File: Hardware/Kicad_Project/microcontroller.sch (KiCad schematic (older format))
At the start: 52 parts

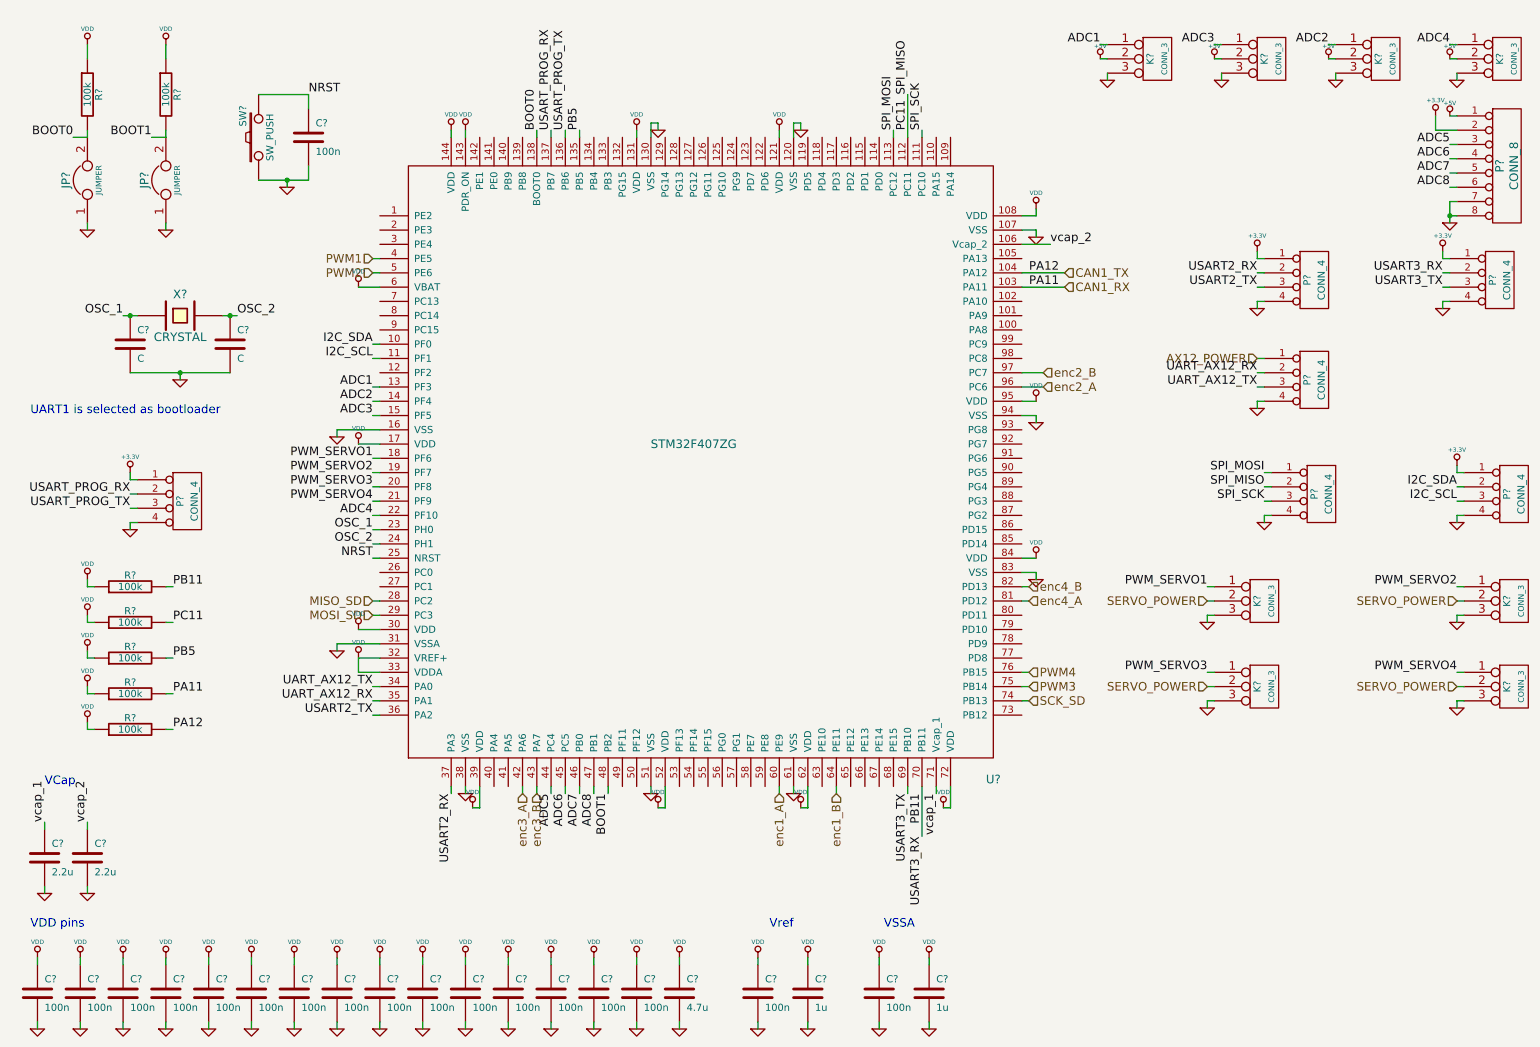
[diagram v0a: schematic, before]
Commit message: [HARDWARE] Add DAC interface
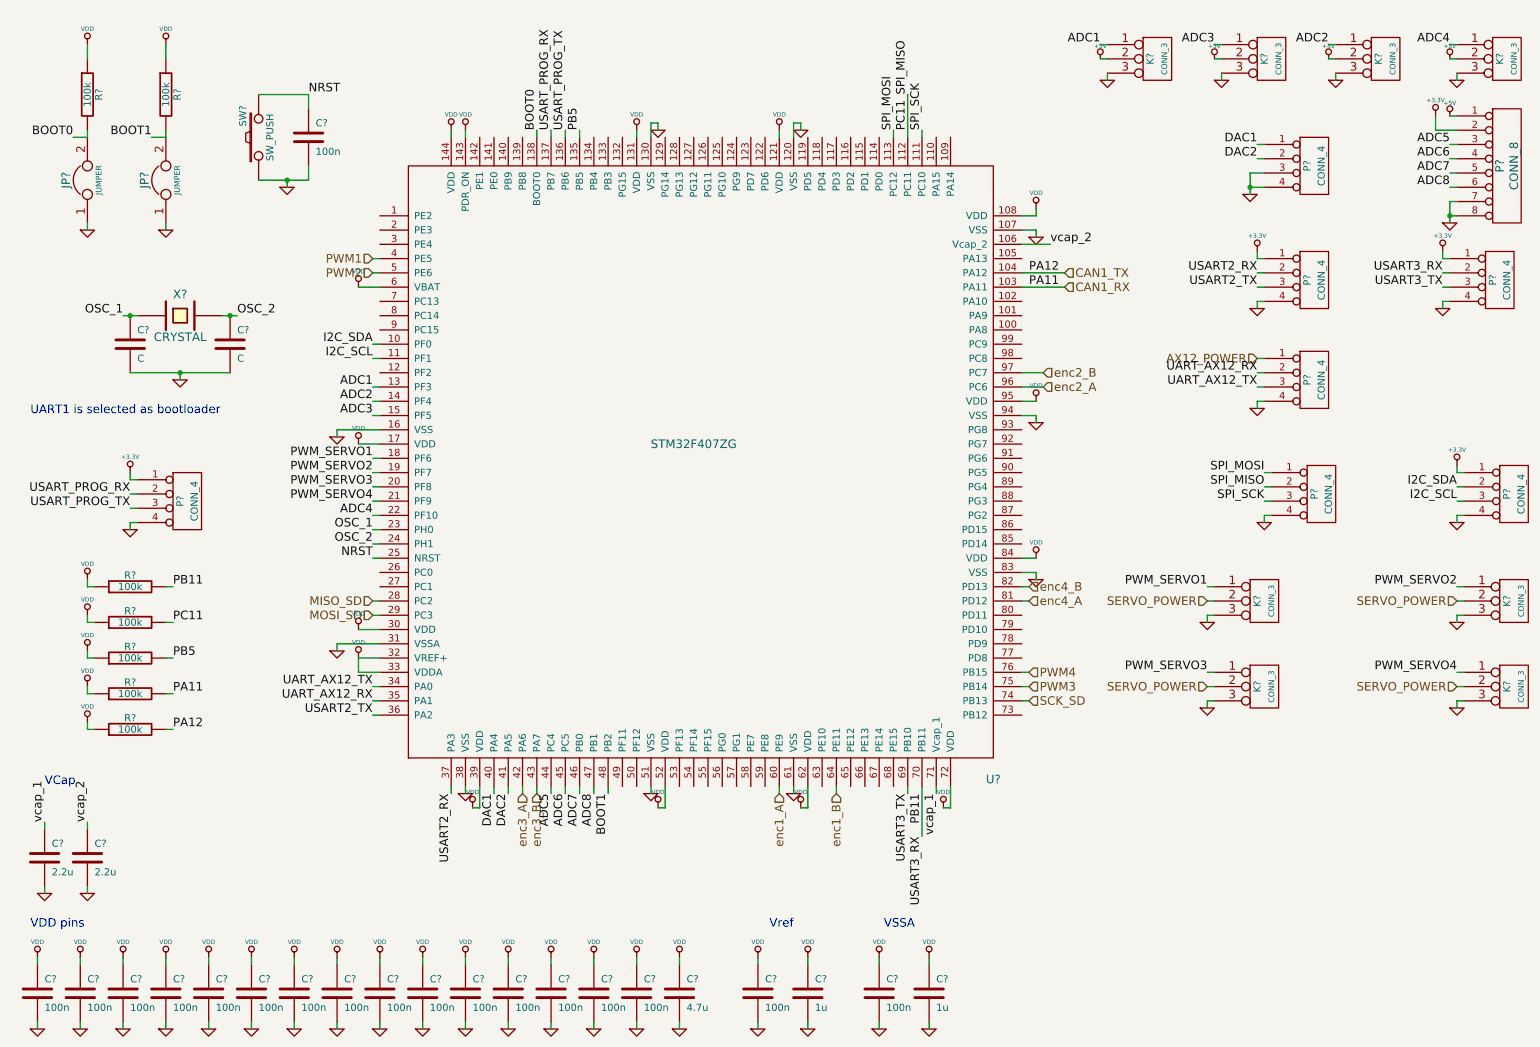
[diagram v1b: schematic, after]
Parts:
- added P?: CONN_4, symbol CONN_4
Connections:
- net GND: now also P?.3 (P3), P?.4 (P4)
- net DAC1: now reaches U?.40 (PA4)
- net DAC1: now also P?.1 (P1)
- net DAC2: now reaches U?.41 (PA5)
- net DAC2: now also P?.2 (P2)
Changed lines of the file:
@@
-EESchema Schematic File Version 2  date mar. 08 oct. 2013 19:30:07 CEST
+EESchema Schematic File Version 2  date mar. 08 oct. 2013 19:33:19 CEST
 LIBS:power
 LIBS:device
@@
 Comment4 ""
 $EndDescr
+Wire Wire Line
+	9150 1500 9200 1500
+Connection ~ 9100 1800
+Wire Wire Line
+	9100 1800 9200 1800
+Wire Wire Line
+	3900 6050 3900 6000
 Connection ~ 10500 2000
 Wire Wire Line
@@
 Wire Wire Line
 	10500 1900 10550 1900
+Wire Wire Line
+	3800 6050 3800 6000
+Wire Wire Line
+	9100 1850 9100 1700
+Wire Wire Line
+	9100 1700 9200 1700
+Wire Wire Line
+	9150 1600 9200 1600
 $Comp
 L GND #PWR?
+U 1 1 525441BE
+P 9100 1850
+F 0 "#PWR?" H 9100 1850 30  0001 C CNN
+F 1 "GND" H 9100 1780 30  0001 C CNN
+	1    9100 1850
+	1    0    0    -1
+$EndComp
+Text Label 9150 1600 2    60   ~ 0
+DAC2
+Text Label 9150 1500 2    60   ~ 0
+DAC1
+$Comp
+L CONN_4 P?
+U 1 1 525441AE
+P 9550 1650
+F 0 "P?" V 9500 1650 50  0000 C CNN
+F 1 "CONN_4" V 9600 1650 50  0000 C CNN
+	1    9550 1650
+	1    0    0    -1
+$EndComp
+Text Label 3900 6050 3    60   ~ 0
+DAC2
+Text Label 3800 6050 3    60   ~ 0
+DAC1
+$Comp
+L GND #PWR?

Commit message: [HARDWARE] Add motor control signals around STM32
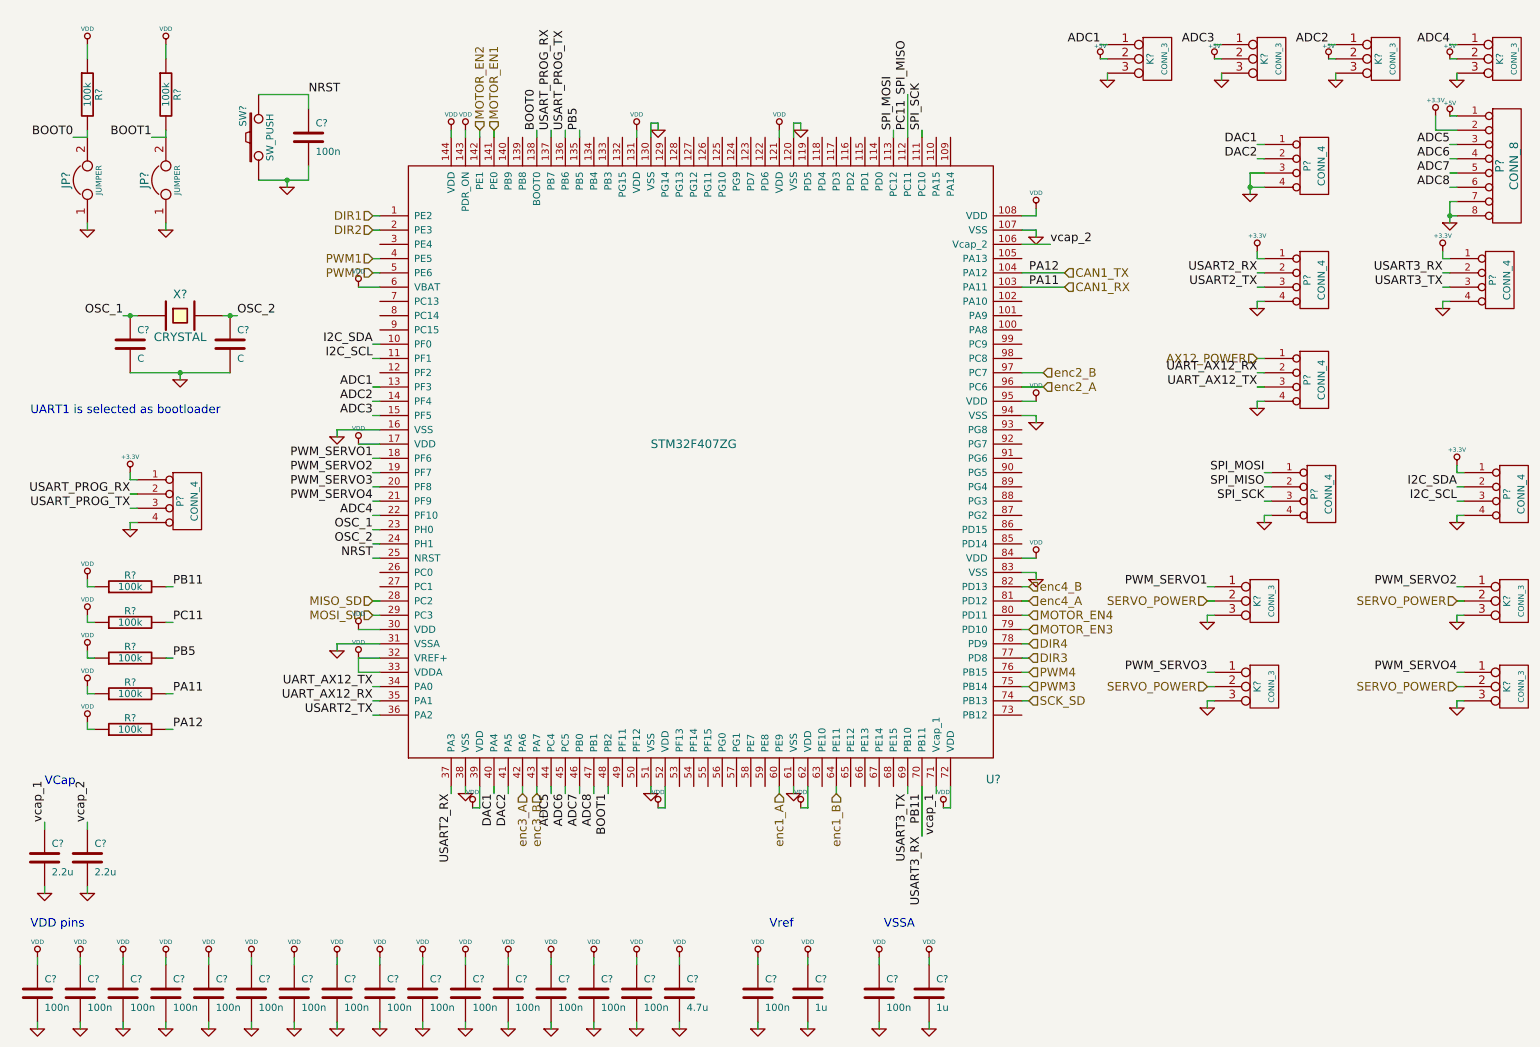
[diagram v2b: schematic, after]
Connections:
- net DIR1: now reaches U?.1 (PE2)
- net MOTOR_EN1: now reaches U?.141 (PE0)
- net MOTOR_EN2: now reaches U?.142 (PE1)
- net DIR2: now reaches U?.2 (PE3)
- net DIR3: now reaches U?.77 (PD8)
- net DIR4: now reaches U?.78 (PD9)
- net MOTOR_EN3: now reaches U?.79 (PD10)
- net MOTOR_EN4: now reaches U?.80 (PD11)
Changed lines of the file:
@@
-EESchema Schematic File Version 2  date mar. 08 oct. 2013 19:33:19 CEST
+EESchema Schematic File Version 2  date mar. 08 oct. 2013 19:41:25 CEST
 LIBS:power
 LIBS:device
@@
 $Descr A4 11700 8267
 encoding utf-8
-Sheet 5 5
+Sheet 2 5
 Title ""
 Date "8 oct 2013"
@@
 $EndDescr
 Wire Wire Line
+	7500 5100 7550 5100
+Wire Wire Line
+	7500 4900 7550 4900
+Wire Wire Line
+	3700 1400 3700 1450
+Wire Wire Line
+	2950 2100 3000 2100
+Wire Wire Line
 	9150 1500 9200 1500
 Connection ~ 9100 1800
@@
 Wire Wire Line
 	9150 1600 9200 1600
+Wire Wire Line
+	3000 2000 2950 2000
+Wire Wire Line
+	3800 1400 3800 1450
+Wire Wire Line
+	7550 4800 7500 4800
+Wire Wire Line
+	7550 5000 7500 5000
+Text HLabel 7550 4800 2    60   Input ~ 0
+MOTOR_EN4
+Text HLabel 7550 4900 2    60   Input ~ 0
+MOTOR_EN3
+Text HLabel 7550 5000 2    60   Input ~ 0
+DIR4
+Text HLabel 7550 5100 2    60   Input ~ 0
+DIR3
+Text HLabel 3700 1400 1    60   Input ~ 0
+MOTOR_EN2
+Text HLabel 3800 1400 1    60   Input ~ 0
+MOTOR_EN1
+Text HLabel 2950 2100 0    60   Input ~ 0
+DIR2
+Text HLabel 2950 2000 0    60   Input ~ 0
+DIR1
 $Comp
 L GND #PWR?

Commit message: [HARDWARE] Finalize SD interface
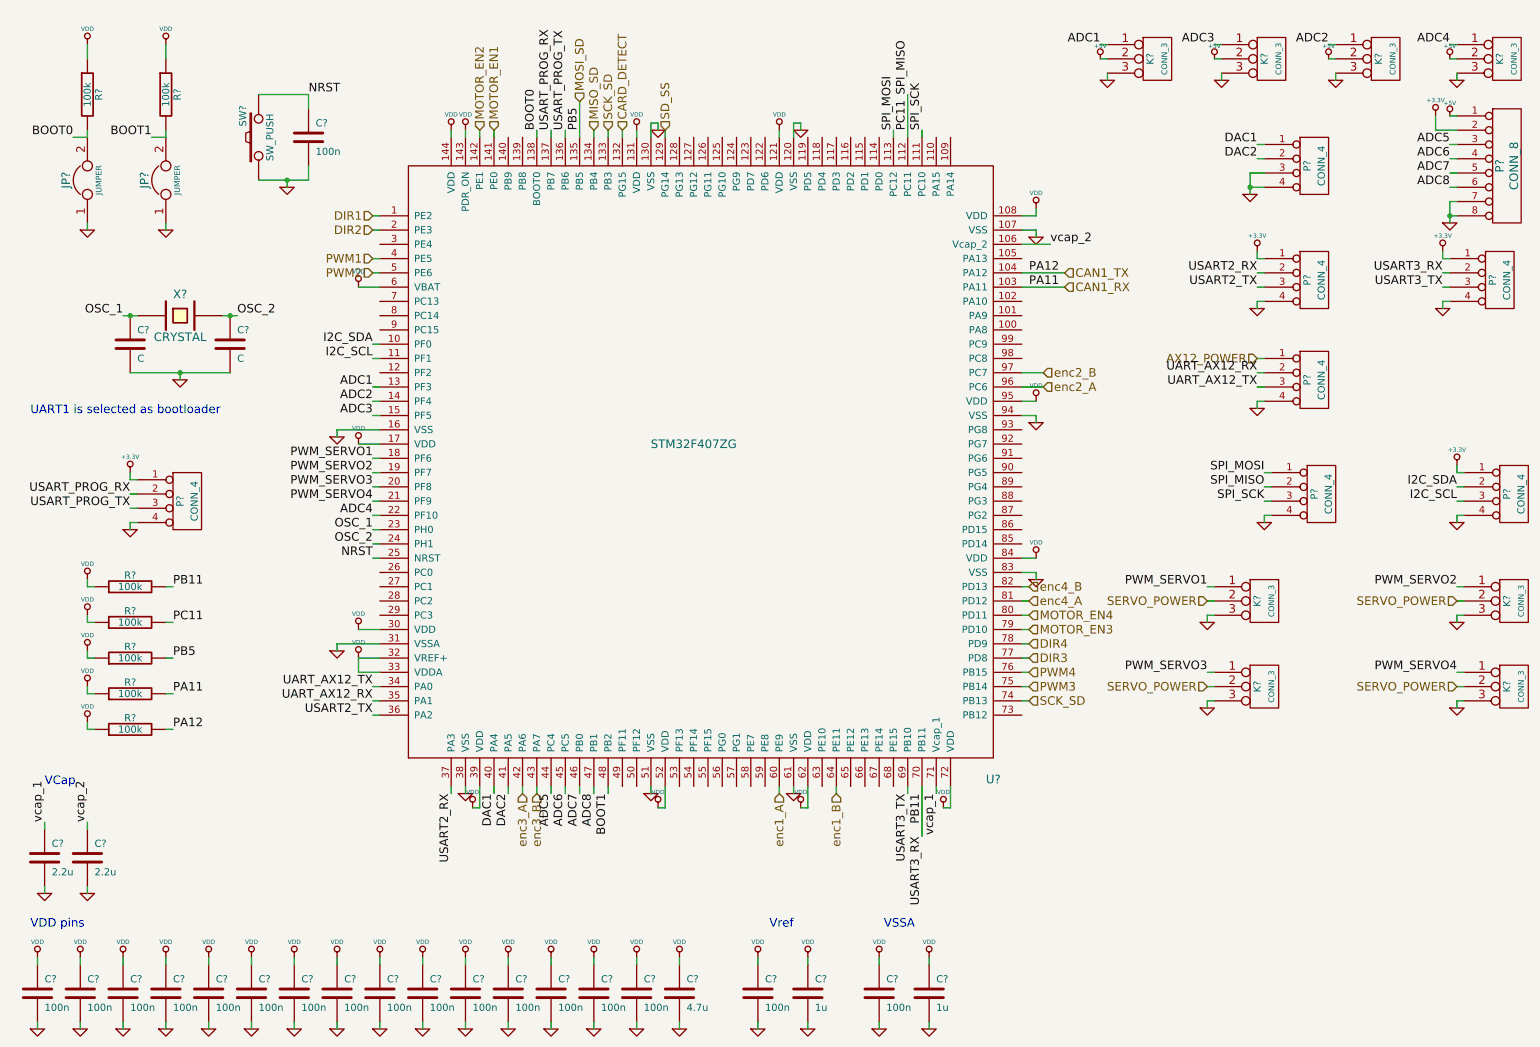
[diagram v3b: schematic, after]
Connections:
- net PB5 is gone; now on net MOSI_SD: R?.2, U?.135 (PB5)
- net MISO_SD: now also U?.134 (PB4); no longer U?.28 (PC2)
- net MOSI_SD: no longer U?.29 (PC3)
- net SCK_SD: now also U?.133 (PB3)
- net SD_SS: now reaches U?.129 (PG14)
- net CARD_DETECT: now reaches U?.132 (PG15)
